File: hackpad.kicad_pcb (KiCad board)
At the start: 2 copper layers, 85.5 x 61 mm, 20 parts, among them J2 Conn_01x04_Pin, SW1 SW_Push_45deg, SW2 SW_Push_45deg, SW3 SW_Push_45deg, SW4 RotaryEncoder_Switch, SW5 SW_Push_45deg, SW6 SW_Push_45deg, SW9 SW_Push_45deg, U1 MOUDLE-SEEEDUINO-XIAO

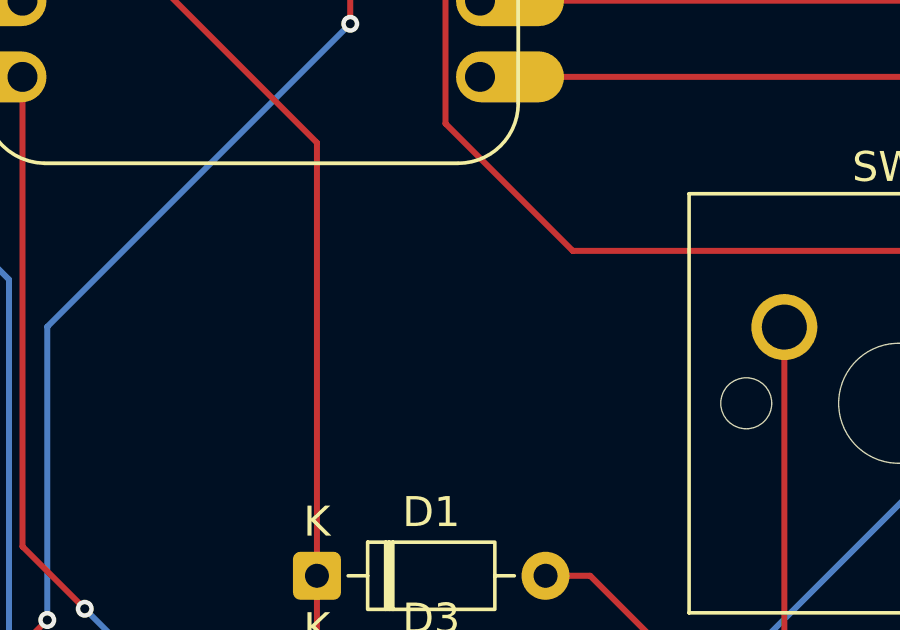
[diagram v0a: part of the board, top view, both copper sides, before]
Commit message: Completed the pcb and added 2 extra leds in the schematic !
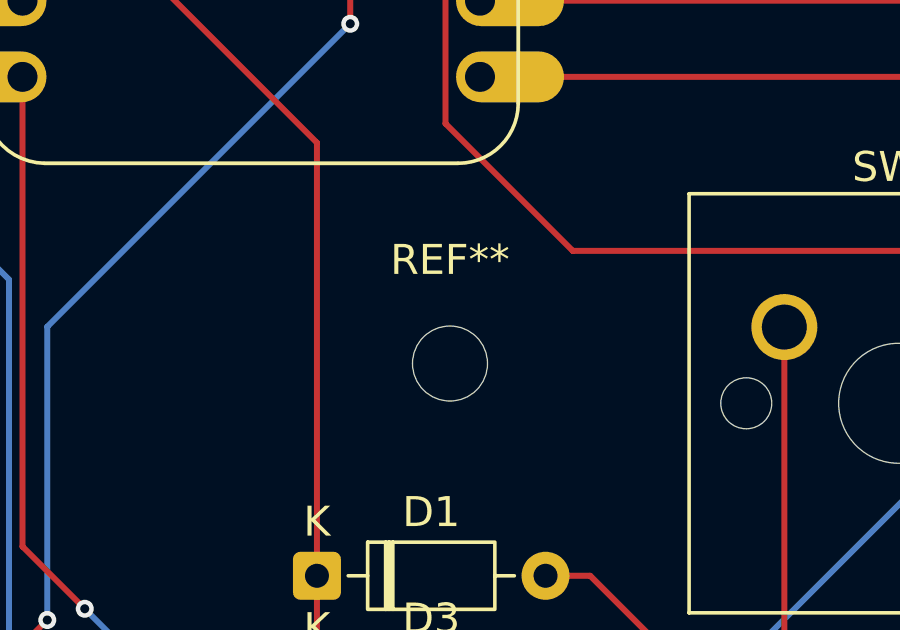
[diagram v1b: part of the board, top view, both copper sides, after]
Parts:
- added REF**: MountingHole_2.5mm, MountingHole:MountingHole_2.5mm, F.Cu at (103.6, 80.7)
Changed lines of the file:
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@@
 		)
+	)
+	(footprint "MountingHole:MountingHole_2.5mm"
+		(layer "F.Cu")
+		(at 103.625 80.675)
+		(descr "Mounting Hole 2.5mm, no annular, generated by kicad-footprint-generator mountinghole.py")
+		(tags "mountinghole")
+		(property "Reference" "REF**"
+			(at 0 -3.45 0)
+			(layer "F.SilkS")
+			(effects
+				(font
+					(size 1 1)
+					(thickness 0.15)
+				)
+			)
+		)
+		(property "Value" "MountingHole_2.5mm"
+			(at 0 3.45 0)
+			(layer "F.Fab")
+			(effects
+				(font
+					(size 1 1)
+					(thickness 0.15)
+				)
+			)
+		)
+		(property "Datasheet" ""
+			(at 0 0 0)
+			(layer "F.Fab")
+			(hide yes)
+			(effects
+				(font
+					(size 1.27 1.27)
+				)
+			)
+		)
+		(property "Description" ""
+			(at 0 0 0)
+			(layer "F.Fab")
+			(hide yes)
+			(effects
+				(font
+					(size 1.27 1.27)
+				)
+			)
+		)
+		(property "KiLib_Generator" "mounting_hardware/mounting_hole"
+			(at 0 0 0)
+			(layer "F.SilkS")
+			(hide yes)
+			(effects
+				(font
+					(size 1 1)
+					(thickness 0.15)
+				)
+			)
+		)
+		(attr exclude_from_pos_files exclude_from_bom)
+		(duplicate_pad_numbers_are_jumpers no)
+		(fp_circle
+			(center 0 0)
+			(end 2.5 0)
+			(stroke
+				(width 0.15)
+				(type solid)
+			)
+			(fill no)
+			(layer "Cmts.User")
+		)
+		(fp_circle
+			(center 0 0)
+			(end 2.75 0)
+			(stroke
+				(width 0.05)
+				(type solid)
+			)
+			(fill no)
+			(layer "F.CrtYd")
+		)
+		(fp_text user "${REFERENCE}"
+			(at 0 0 0)
+			(layer "F.Fab")
+			(effects
+				(font
+					(size 1 1)
+					(thickness 0.15)
+				)
+			)
+		)
+		(pad "" np_thru_hole circle
+			(at 0 0)
+			(size 2.5 2.5)
+			(drill 2.5)
+			(layers "*.Cu" "*.Mask")
+		)
+		(embedded_fonts no)
 	)
 	(footprint "Connector_PinHeader_2.54mm:PinHeader_1x04_P2.54mm_Vertical"
